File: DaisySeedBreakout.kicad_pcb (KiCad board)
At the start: 2 copper layers, 56.1 x 65 mm, 164 parts, among them J1 Conn_01x03, J10 Conn_01x02, J11 Conn_01x02, J12 Conn_01x02, J13 Conn_01x02, J14 Conn_01x02, J20 Conn_01x02, J21 Conn_01x02, J22 Conn_01x02, J24 Conn_01x02, J25 Conn_01x02, J26 Conn_02x04, J27 Conn_01x03, J3 Conn_01x03, J30 Conn_01x02, J31 Conn_02x04, J32 Conn_01x02, J33 Conn_01x02, J34 Conn_01x02, J35 Conn_01x02, J4 5027740891, J47 Conn_01x03, J48 Conn_01x03, J49 Conn_01x03, J50 Conn_01x03, J51 Conn_01x03, J52 Conn_01x03, J53 Conn_01x03, J54 Conn_01x03, J55 Conn_01x03, J56 Conn_01x03, J57 Conn_01x03, J58 Conn_01x03, J59 Conn_01x03, J6 Conn_01x02, J60 Conn_01x03, J61 Conn_01x03, J62 Conn_01x03, J63 Conn_01x03, J64 Conn_01x03, J65 Conn_01x03, J66 Conn_01x02, J67 Conn_01x02, J68 Conn_01x02, J69 Conn_01x02, J70 Conn_01x02, J8 Conn_01x02, J9 Conn_01x02, U1 H11L1M, U2 PAM8320RDR, U4 ATMEGA1608-MFR, U5 MAX9814, U6 DSC6001CE2A-010.0000

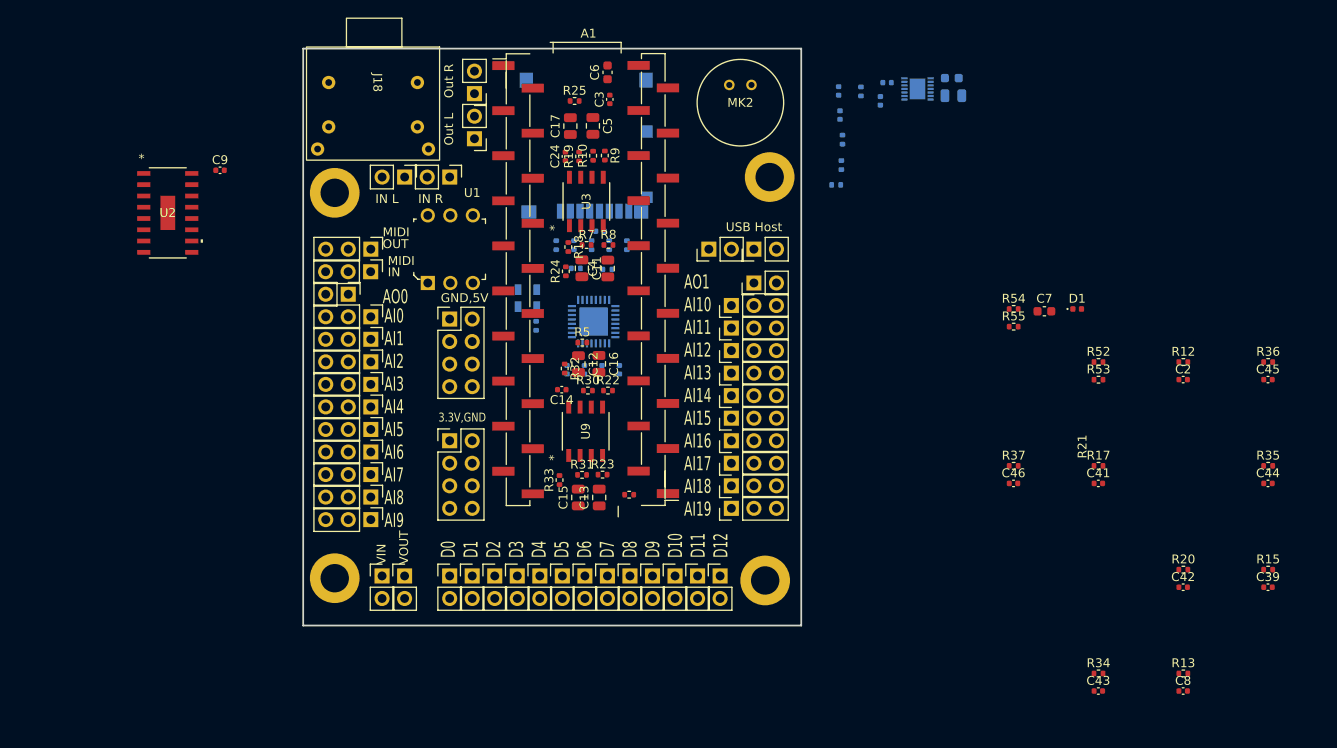
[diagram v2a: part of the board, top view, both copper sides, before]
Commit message: add input fuse holder, TVS, reverse diode protection, placeholder 5V LDO
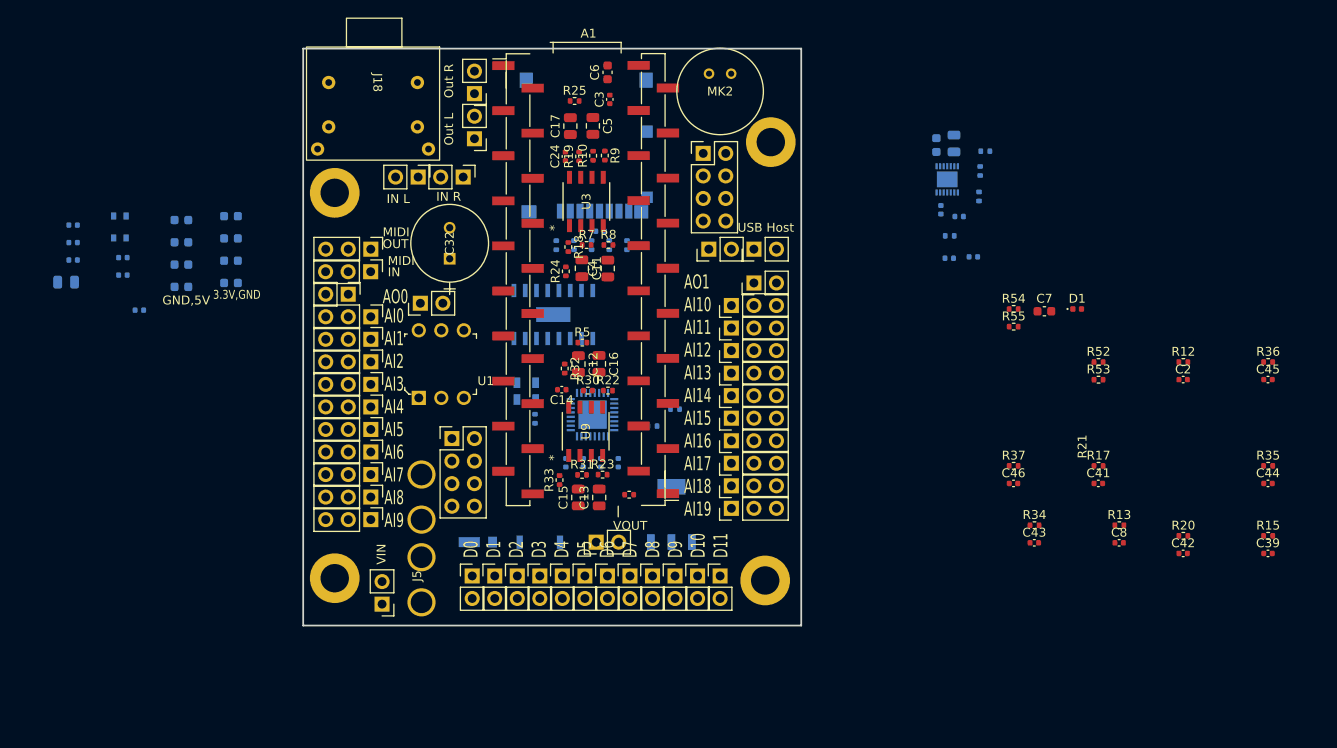
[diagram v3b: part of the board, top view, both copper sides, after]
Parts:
- removed J66: Conn_01x02, Ultralibrarian:PinHeader_1x02_P2.54mm_Vertical_Female
- added C10: 220pF, Capacitor_SMD:C_0402_1005Metric, B.Cu at (87.6, 55.6)
- added C25: 220pF, Capacitor_SMD:C_0402_1005Metric, B.Cu at (87.6, 57.5)
- added C26: 1u, Capacitor_SMD:C_0603_1608Metric, B.Cu at (99.8, 50.9)
- added C27: 1u, Capacitor_SMD:C_0603_1608Metric, B.Cu at (99.8, 53.4)
- added C28: 1u, Capacitor_SMD:C_0603_1608Metric, B.Cu at (99.8, 55.9)
- added C29: 1u, Capacitor_SMD:C_0603_1608Metric, B.Cu at (99.8, 58.4)
- added C30: 1u, Capacitor_SMD:C_0603_1608Metric, B.Cu at (94.2, 51.3)
- added C32: 860020474014, 470uF:CAP_WCAP-ATG5_8x11.5_WRE, F.Cu at (124.5, 55.7)
- added C33: 0.1uF, Capacitor_SMD:C_0603_1608Metric, B.Cu at (94.2, 53.8)
- added C34: 0.1uF, Capacitor_SMD:C_0603_1608Metric, B.Cu at (94.2, 56.3)
- added C35: 0.1uF, Capacitor_SMD:C_0603_1608Metric, B.Cu at (94.2, 58.9)
- added C57: 0.1uF, Capacitor_SMD:C_0402_1005Metric, B.Cu at (82.0, 51.9)
- added C58: 0.1uF, Capacitor_SMD:C_0402_1005Metric, B.Cu at (82.0, 53.9)
- added C59: 0.1uF, Capacitor_SMD:C_0402_1005Metric, B.Cu at (82.0, 55.8)
- added C60: 47uF, Capacitor_SMD:C_0805_2012Metric, B.Cu at (81.2, 58.3)
- added CR1: DFLT15A-7, TVSDiode:ZDO_POWERDI123_DIO, B.Cu at (127.6, 87.6)
- added FB1: MPZ1608S221ATA00, digikey-footprints:0603, B.Cu at (87.3, 50.9)
- added FB2: MPZ1608S221ATA00, digikey-footprints:0603, B.Cu at (87.3, 53.3)
- added J2: Conn_01x02, Connector_PinHeader_2.54mm:PinHeader_1x02_P2.54mm_Vertical, F.Cu at (121.2, 60.7)
- added J5: ~, Ultralibrarian:BladeFuseHolder, F.Cu at (121.3, 87.6)
- added R56: RSX501LAM20TR, 5ADiode:DIO_RB050LAM_ROM, B.Cu at (134.6, 87.6)
- added U7: LM317MDCYR, WideInputRangeLdo:DCY4, B.Cu at (149.5, 84.5)
- C9, U2: moved to B.Cu
- moved U2 44.9 mm to (136.1, 62.0), turned to 90 degrees
- moved J31 43.2 mm to (153.0, 43.8)
- moved J34 24.4 mm to (141.0, 87.6), turned to 90 degrees
- moved C19 22.6 mm to (180.8, 55.6), turned to 180 degrees
- moved C21 21.9 mm to (183.5, 55.5), turned to 0 degrees
- moved R11 19.4 mm to (149.9, 72.6)
- moved R29 19.1 mm to (180.8, 53.1), turned to 180 degrees
- moved R6 18.4 mm to (147.3, 74.5)
- moved C9 18.2 mm to (89.5, 61.5), turned to 180 degrees
- moved R13 18.2 mm to (199.9, 85.7)
- moved R34 18.2 mm to (190.4, 85.7)
- moved C43 18.2 mm to (190.4, 87.7)
- moved C8 18.2 mm to (199.9, 87.7)
- moved R27 17.2 mm to (184.8, 43.6), turned to 180 degrees
- moved R28 16.7 mm to (184.1, 48.7), turned to 90 degrees
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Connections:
- net +5V_ISO renamed +5V
- A1 pad 39: +9V -> +12V
- C6 pad 1: +9V -> +12V
- J34 pad 1: unconnected-(J34-Pin_1-Pad1) -> +12V
- J34 pad 2: unconnected-(J34-Pin_2-Pad2) -> GND
- J35 pad 1: unconnected-(J35-Pin_1-Pad1) -> Net-(J35-Pin_1)
- J35 pad 2: unconnected-(J35-Pin_2-Pad2) -> GND
- U2 pad 1: unconnected-(U2-PVCCN-Pad1) -> +12V
- U2 pad 10: unconnected-(U2-OUTP-Pad10) -> Net-(U2-OUTP)
- U2 pad 11: unconnected-(U2-BSP-Pad11) -> Net-(U2-BSP)
- U2 pad 12: unconnected-(U2-MUTE-Pad12) -> GND
- U2 pad 13: unconnected-(U2-AVCC-Pad13) -> +12V
- U2 pad 14: unconnected-(U2-BSN-Pad14) -> Net-(U2-BSN)
- U2 pad 15: unconnected-(U2-OUTN-Pad15) -> Net-(U2-OUTN)
- U2 pad 16: unconnected-(U2-PGNDN-Pad16) -> GND
- U2 pad 2: unconnected-(U2-SDN-Pad2) -> /SPEAKER_SHUTDOWN_N
- U2 pad 3: unconnected-(U2-IN-Pad3) -> Net-(U2-IN)
- U2 pad 4: unconnected-(U2-VCM-Pad4) -> Net-(U2-VCM)
- U2 pad 5: unconnected-(U2-AGND-Pad5) -> GND
- U2 pad 6: unconnected-(U2-AGND-Pad6) -> GND
- U2 pad 7: unconnected-(U2-VCLAMP-Pad7) -> Net-(U2-VCLAMP)
- U2 pad 8: unconnected-(U2-PVCCP-Pad8) -> +12V
- U2 pad 9: unconnected-(U2-PGNDP-Pad9) -> GND
- U4 pad 31: /GPIO_Conn10/GPIO_Conn -> /SPEAKER_SHUTDOWN_N
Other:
- board text added: "D0 D1 D2 D3 D4 D5 D6 D7 D8 D9 D10 D11"
- board text removed: "D0 D1 D2 D3 D4 D5 D6 D7 D8 D9 D10 D11 D12"

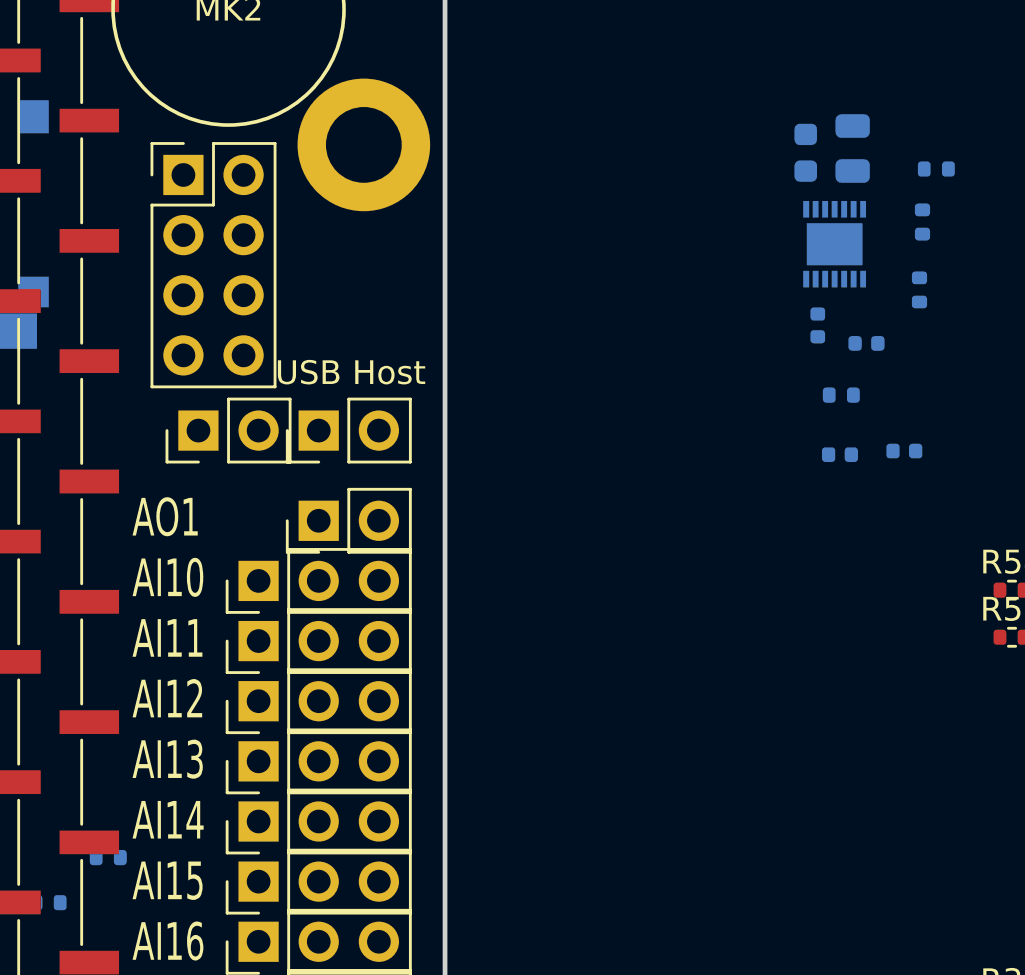
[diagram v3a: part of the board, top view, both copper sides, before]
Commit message: add usb host current limit and ESD diodes
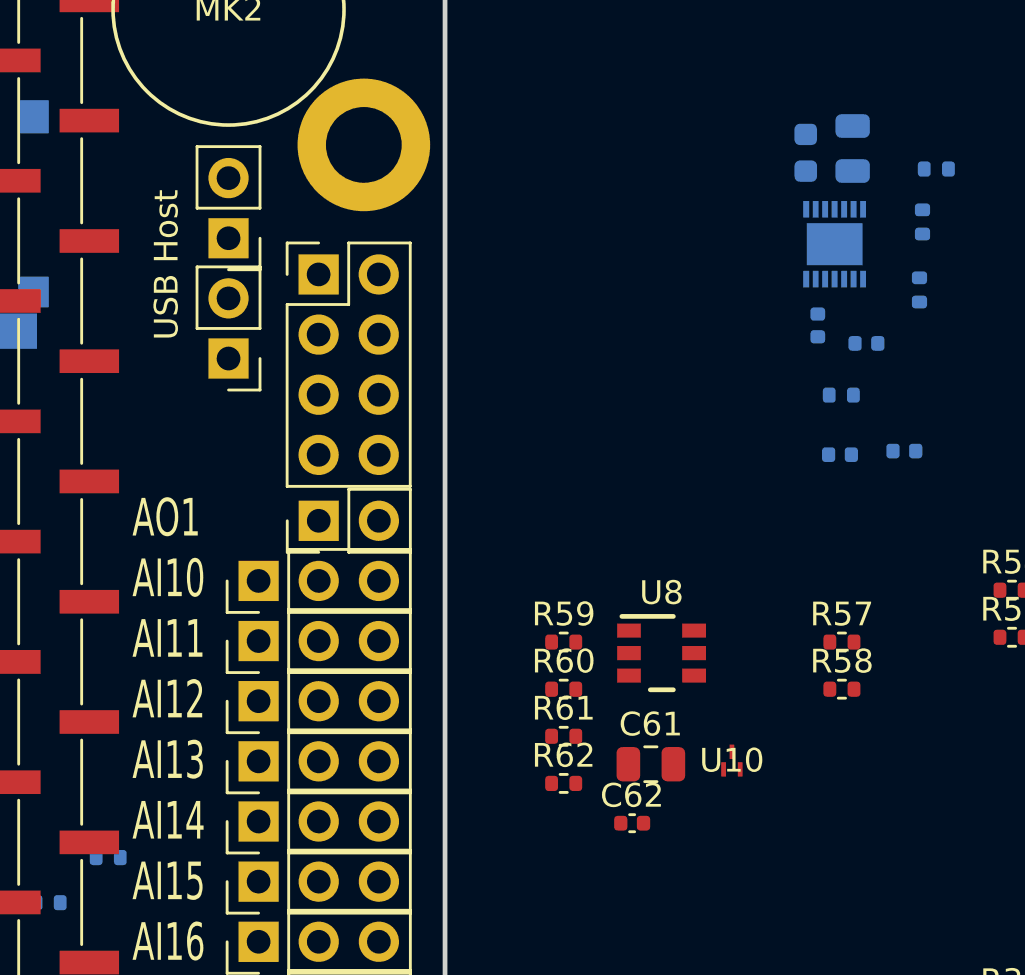
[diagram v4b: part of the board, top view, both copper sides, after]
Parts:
- added C61: 47uF, Capacitor_SMD:C_0805_2012Metric, F.Cu at (172.8, 68.7)
- added C62: 0.1uF, Capacitor_SMD:C_0402_1005Metric, F.Cu at (172.0, 71.2)
- added R57: 4.7k, Resistor_SMD:R_0402_1005Metric, F.Cu at (180.8, 63.5)
- added R58: 4.7k, Resistor_SMD:R_0402_1005Metric, F.Cu at (180.8, 65.5)
- added R59: 23k, Resistor_SMD:R_0402_1005Metric, F.Cu at (169.1, 63.5)
- added R60: 23k, Resistor_SMD:R_0402_1005Metric, F.Cu at (169.1, 65.5)
- added R61: 2.2k, Resistor_SMD:R_0402_1005Metric, F.Cu at (169.1, 67.5)
- added R62: 0, Resistor_SMD:R_0402_1005Metric, F.Cu at (169.1, 69.5)
- added U10: TPD2EUSB30ADRTR, USB_ESD:DRT3, F.Cu at (176.2, 68.5)
- added U8: TPS2553DBVR-1, USB_Current_Limit:DBV0006A_N, F.Cu at (173.2, 64.0)
- moved J32 8.97 mm to (154.9, 46.5), turned to 180 degrees
- moved J31 7.09 mm to (158.7, 48.0)
- moved J33 3.30 mm to (154.9, 51.6), turned to 180 degrees
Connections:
- A1 pad 1: unconnected-(A1-USB_ID-Pad1) -> Net-(A1-USB_ID)
- A1 pad 36: unconnected-(A1-USB_D_--Pad36) -> /USB_n
- A1 pad 37: unconnected-(A1-USB_D_+-Pad37) -> /USB_p
- C29 pad 2: GND -> Net-(U2-OUTP)
- C30 pad 2: GND -> Net-(U2-OUTN)
- J26 pad 1: unconnected-(J26-Pin_1-Pad1) -> GND
- J26 pad 2: unconnected-(J26-Pin_2-Pad2) -> +5V
- J26 pad 3: unconnected-(J26-Pin_3-Pad3) -> GND
- J26 pad 4: unconnected-(J26-Pin_4-Pad4) -> +5V
- J26 pad 5: unconnected-(J26-Pin_5-Pad5) -> GND
- J26 pad 6: unconnected-(J26-Pin_6-Pad6) -> +5V
- J26 pad 7: unconnected-(J26-Pin_7-Pad7) -> GND
- J26 pad 8: unconnected-(J26-Pin_8-Pad8) -> +5V
- J31 pad 1: unconnected-(J31-Pin_1-Pad1) -> GND
- J31 pad 2: unconnected-(J31-Pin_2-Pad2) -> +3.3V
- J31 pad 3: unconnected-(J31-Pin_3-Pad3) -> GND
- J31 pad 4: unconnected-(J31-Pin_4-Pad4) -> +3.3V
- J31 pad 5: unconnected-(J31-Pin_5-Pad5) -> GND
- J31 pad 6: unconnected-(J31-Pin_6-Pad6) -> +3.3V
- J31 pad 7: unconnected-(J31-Pin_7-Pad7) -> GND
- J31 pad 8: unconnected-(J31-Pin_8-Pad8) -> +3.3V
- J32 pad 1: unconnected-(J32-Pin_1-Pad1) -> /USB_p
- J32 pad 2: unconnected-(J32-Pin_2-Pad2) -> GND
- J33 pad 1: unconnected-(J33-Pin_1-Pad1) -> Net-(J33-Pin_1)
- J33 pad 2: unconnected-(J33-Pin_2-Pad2) -> /USB_n

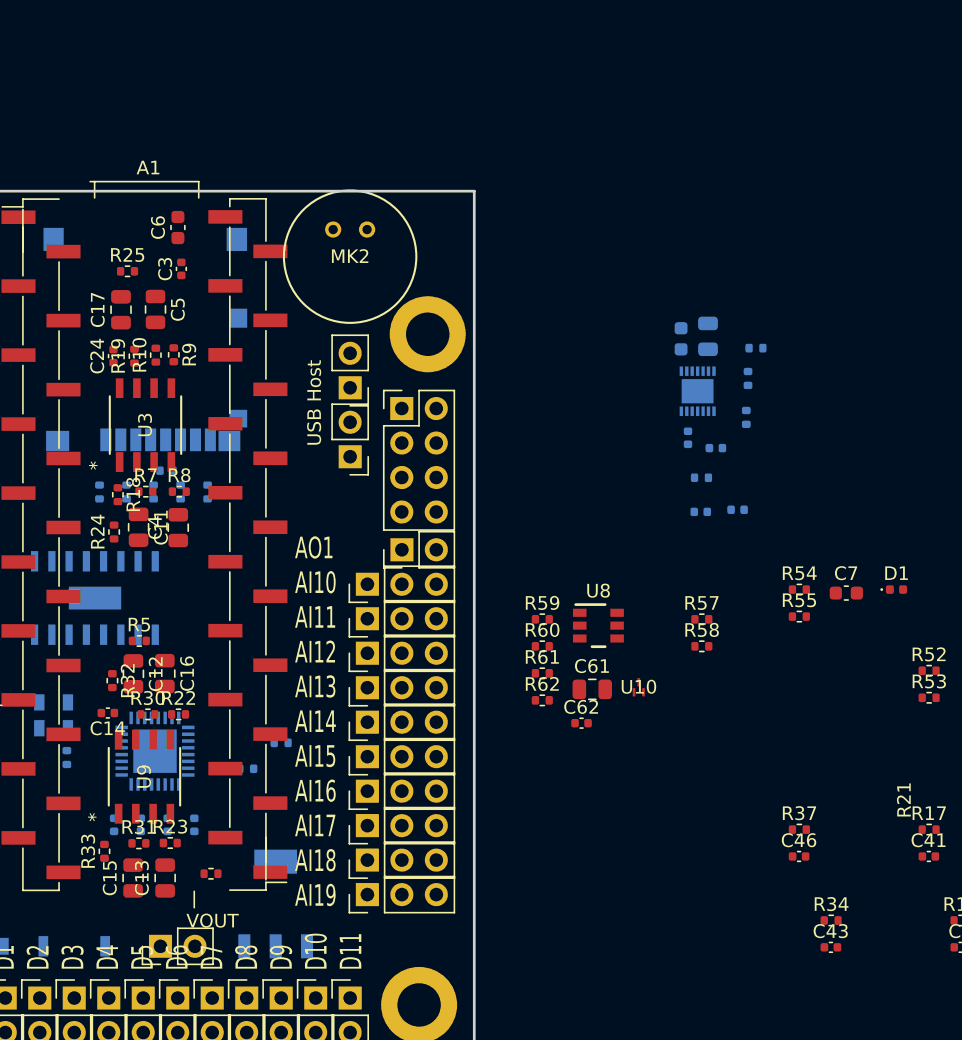
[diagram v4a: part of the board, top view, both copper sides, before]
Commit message: Add USB 5V switcher, adjust audio in circuit
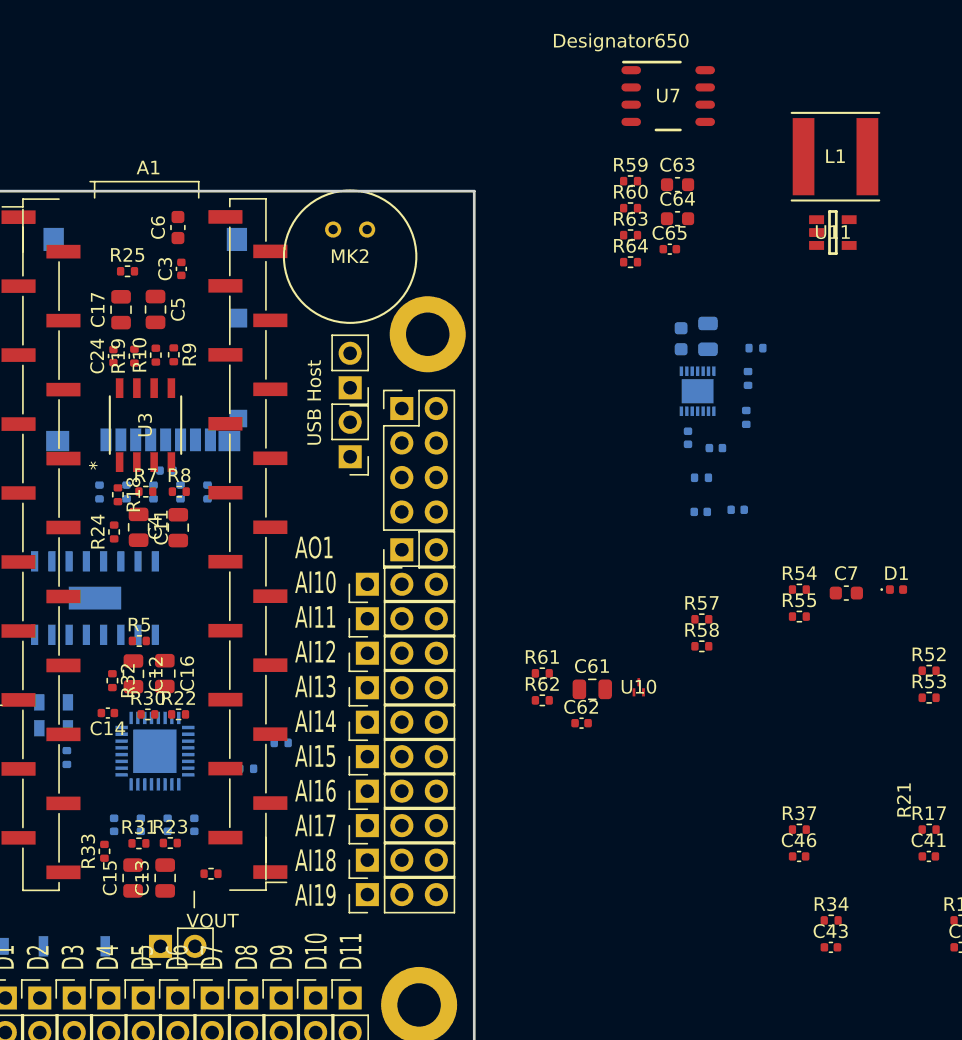
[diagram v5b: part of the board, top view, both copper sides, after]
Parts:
- removed U8: TPS2553DBVR-1, USB_Current_Limit:DBV0006A_N
- removed U9: ~, Ultralibrarian:D8_TEX
- added C63: 10uF, Capacitor_SMD:C_0603_1608Metric, F.Cu at (179.1, 31.5)
- added C64: 10uF, Capacitor_SMD:C_0603_1608Metric, F.Cu at (179.1, 34.0)
- added C65: 0.1uF, Capacitor_SMD:C_0402_1005Metric, F.Cu at (178.5, 36.3)
- added L1: 10uH 1.9A ASPI-0628-100M-T1, 10uHInductor:ASPI-0628_ASPI-0628-4R7M-T1_ABR, F.Cu at (190.7, 29.5)
- added R63: TBD, Resistor_SMD:R_0402_1005Metric, F.Cu at (175.6, 35.2)
- added R64: TBD, Resistor_SMD:R_0402_1005Metric, F.Cu at (175.6, 37.2)
- added U11: TPS560200DBVR, USB_Switcher:DBV0005A_N, F.Cu at (190.5, 35.1)
- R59, R60: value 23k -> TBD
- U7: value LM317MDCYR -> TLV9062IDR; footprint WideInputRangeLdo:DCY4 -> TLV9062:D0008A_N; moved to F.Cu
- moved U7 66.2 mm to (178.4, 25.0), turned to 0 degrees
- moved R59 32.9 mm to (175.6, 31.3)
- moved R60 32.9 mm to (175.6, 33.3)
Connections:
- A1 pad 21: Net-(A1-3V3_A) -> +3.3VA
- C12 pad 2: Net-(U9B-+IN_B) -> Net-(U7B-IN+)
- C13 pad 2: Net-(U9A-+IN_A) -> Net-(U7A-IN-)
- C14 pad 1: +5V -> +3.3VA
- C15 pad 2: Net-(U9A-+IN_A) -> Net-(U7A-IN-)
- C16 pad 2: Net-(U9B-+IN_B) -> Net-(U7B-IN+)
- C24 pad 1: +5V -> +12V
- C61 pad 1: Net-(J33-Pin_1) -> +5V
- C62 pad 1: Net-(J33-Pin_1) -> +5V
- C9 pad 1: Net-(A1-3V3_A) -> +3.3VA
- J33 pad 1: Net-(J33-Pin_1) -> +5V
- R22 pad 1: Net-(U9B-+IN_B) -> Net-(U7B-IN+)
- R23 pad 1: Net-(U9A-+IN_A) -> Net-(U7A-IN-)
- R30 pad 1: +5V -> +3.3VA
- R30 pad 2: Net-(U9B-+IN_B) -> Net-(U7B-IN+)
- R31 pad 1: +5V -> +3.3VA
- R31 pad 2: Net-(U9A-+IN_A) -> Net-(U7A-IN-)
- R32 pad 2: Net-(U9B--B) -> Net-(U7B-IN-)
- R33 pad 2: Net-(U9A--A) -> Net-(U7A-IN+)
- R59 pad 1: Net-(U8-ILIM) -> +12V
- R59 pad 2: GND -> Net-(U11-EN)
- R60 pad 1: +5V -> Net-(U11-EN)
- R60 pad 2: Net-(U8-FAULT_N) -> GND
- R61 pad 1: Net-(J33-Pin_1) -> +5V
- R7 pad 1: +5V -> +12V
- R9 pad 1: +5V -> +12V
- U3 pad 8: +5V -> +12V
- U7 pad 1: +5V -> Net-(U7A-IN+)
- U7 pad 2: +12V -> Net-(U7A-IN-)
- U7 pad 3: +5V -> Net-(U7A-IN+)
- U7 pad 4: unconnected-(U7-ADJUST-Pad4) -> GND
